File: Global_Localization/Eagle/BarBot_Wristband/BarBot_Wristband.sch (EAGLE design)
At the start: 2 parts, among them J1 AVR_SPI_PROG_3X2PTH, U2 DWM1000

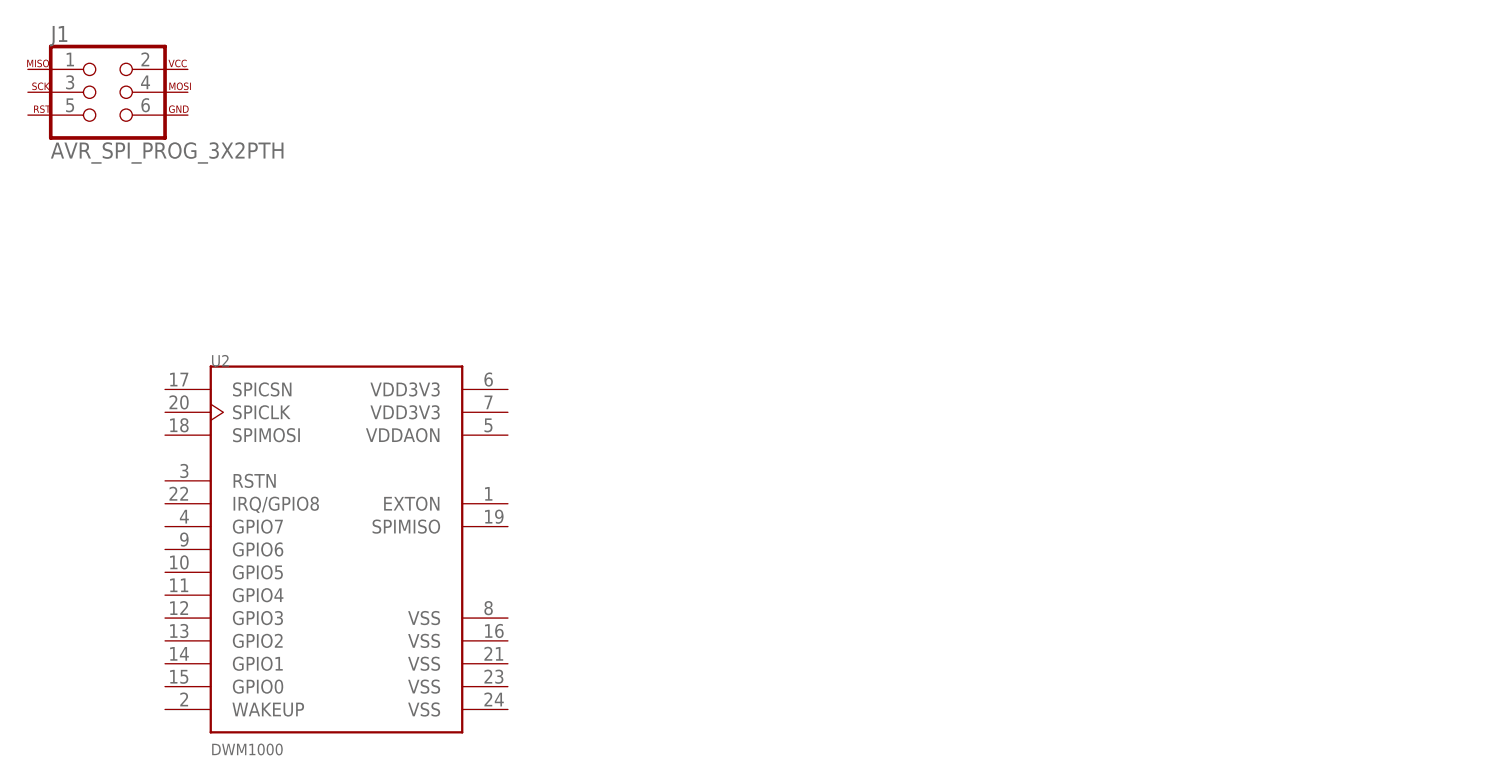
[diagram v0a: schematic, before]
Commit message: Updated board for wristband to be arduino shield
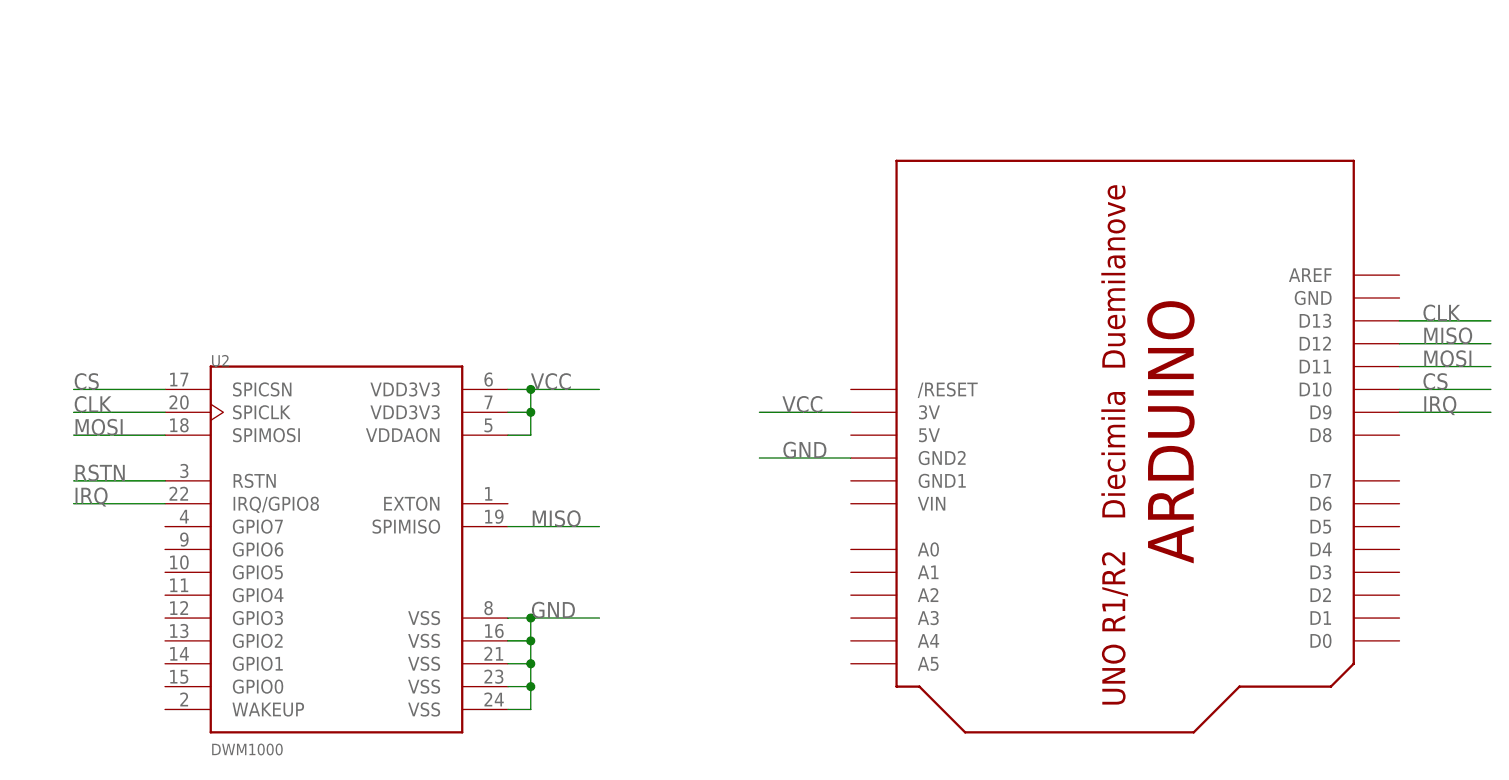
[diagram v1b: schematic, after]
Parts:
- removed J1: AVR_SPI_PROG_3X2PTH, SparkFun-Connectors:AVR_SPI_PROG_3X2PTH
- added U$1: ARDUINO-BPLACE, adafruit:ARDUINO-BPLACE
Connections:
- new net CLK: U$1.D13, U2.SPICLK
- new net CS: U$1.D10, U2.SPICSN
- new net GND: U$1.GND2, U2.VSS@1, U2.VSS@2, U2.VSS@3, U2.VSS@4, U2.VSS@5
- new net IRQ: U$1.D9, U2.IRQ/GPIO8
- new net MISO: U$1.D12, U2.SPIMISO
- new net MOSI: U$1.D11, U2.SPIMOSI
- new net RSTN: U2.RSTN
- new net VCC: U$1.3V, U2.VDD3V3@1, U2.VDD3V3@2, U2.VDDAON
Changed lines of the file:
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@@
 <layer number="230" name="230bmp" color="7" fill="1" visible="yes" active="yes"/>
 <layer number="231" name="231bmp" color="7" fill="1" visible="yes" active="yes"/>
+<layer number="232" name="Eagle3D_PG2" color="7" fill="1" visible="no" active="no"/>
+<layer number="233" name="Eagle3D_PG3" color="7" fill="1" visible="no" active="no"/>
 <layer number="248" name="Housing" color="7" fill="1" visible="yes" active="yes"/>
 <layer number="249" name="Edge" color="7" fill="1" visible="yes" active="yes"/>
@@
 <parts>
 <part name="U2" library="DWM1000" deviceset="DWM1000" device=""/>
-<part name="J1" library="SparkFun-Connectors" deviceset="AVR_SPI_PROG_3X2" device="PTH"/>
+<part name="U$1" library="adafruit" deviceset="ARDUINO" device="-BPLACE"/>
 </parts>
 <sheets>
@@
 <instances>
 <instance part="U2" gate="G$1" x="165.1" y="53.34"/>
-<instance part="J1" gate="G$1" x="139.7" y="104.14"/>
+<instance part="U$1" gate="G$1" x="256.54" y="73.66" rot="R270"/>
 </instances>
 <busses>
 </busses>
 <nets>
+<net name="MOSI" class="0">
+<segment>
+<pinref part="U2" gate="G$1" pin="SPIMOSI"/>
+<wire x1="147.32" y1="66.04" x2="137.16" y2="66.04" width="0.1524" layer="91"/>
+<label x="137.16" y="66.04" size="1.778" layer="95"/>
+</segment>
+<segment>
+<pinref part="U$1" gate="G$1" pin="D11"/>
+<wire x1="284.48" y1="73.66" x2="294.64" y2="73.66" width="0.1524" layer="91"/>
+<label x="287.02" y="73.66" size="1.778" layer="95"/>
+</segment>
+</net>
+<net name="CLK" class="0">
+<segment>
+<pinref part="U2" gate="G$1" pin="SPICLK"/>
+<wire x1="147.32" y1="68.58" x2="137.16" y2="68.58" width="0.1524" layer="91"/>
+<label x="137.16" y="68.58" size="1.778" layer="95"/>
+</segment>
+<segment>
+<pinref part="U$1" gate="G$1" pin="D13"/>
+<wire x1="284.48" y1="78.74" x2="294.64" y2="78.74" width="0.1524" layer="91"/>
+<label x="287.02" y="78.74" size="1.778" layer="95"/>
+</segment>
+</net>
+<net name="CS" class="0">
+<segment>
+<pinref part="U2" gate="G$1" pin="SPICSN"/>
+<wire x1="147.32" y1="71.12" x2="137.16" y2="71.12" width="0.1524" layer="91"/>
+<label x="137.16" y="71.12" size="1.778" layer="95"/>
+</segment>
+<segment>
+<pinref part="U$1" gate="G$1" pin="D10"/>
+<wire x1="284.48" y1="71.12" x2="294.64" y2="71.12" width="0.1524" layer="91"/>
+<label x="287.02" y="71.12" size="1.778" layer="95"/>
+</segment>
+</net>
+<net name="IRQ" class="0">
+<segment>
+<pinref part="U2" gate="G$1" pin="IRQ/GPIO8"/>
+<wire x1="147.32" y1="58.42" x2="137.16" y2="58.42" width="0.1524" layer="91"/>
+<label x="137.16" y="58.42" size="1.778" layer="95"/>
+</segment>
+<segment>
+<pinref part="U$1" gate="G$1" pin="D9"/>
+<wire x1="284.48" y1="68.58" x2="294.64" y2="68.58" width="0.1524" layer="91"/>
+<label x="287.02" y="68.58" size="1.778" layer="95"/>
+</segment>
+</net>
+<net name="MISO" class="0">
+<segment>
+<pinref part="U2" gate="G$1" pin="SPIMISO"/>
+<wire x1="185.42" y1="55.88" x2="195.58" y2="55.88" width="0.1524" layer="91"/>
+<label x="187.96" y="55.88" size="1.778" layer="95"/>
+</segment>
+<segment>
+<pinref part="U$1" gate="G$1" pin="D12"/>
+<wire x1="284.48" y1="76.2" x2="294.64" y2="76.2" width="0.1524" layer="91"/>
+<label x="287.02" y="76.2" size="1.778" layer="95"/>
+</segment>
+</net>
+<net name="GND" class="0">
+<segment>
+<pinref part="U2" gate="G$1" pin="VSS@5"/>
+<wire x1="185.42" y1="35.56" x2="187.96" y2="35.56" width="0.1524" layer="91"/>
+<wire x1="187.96" y1="35.56" x2="187.96" y2="38.1" width="0.1524" layer="91"/>
+<wire x1="187.96" y1="38.1" x2="187.96" y2="40.64" width="0.1524" layer="91"/>
+<wire x1="187.96" y1="40.64" x2="187.96" y2="43.18" width="0.1524" layer="91"/>
+<wire x1="187.96" y1="43.18" x2="187.96" y2="45.72" width="0.1524" layer="91"/>
+<wire x1="187.96" y1="45.72" x2="195.58" y2="45.72" width="0.1524" layer="91"/>
+<pinref part="U2" gate="G$1" pin="VSS@1"/>
+<wire x1="185.42" y1="45.72" x2="187.96" y2="45.72" width="0.1524" layer="91"/>
+<junction x="187.96" y="45.72"/>
+<pinref part="U2" gate="G$1" pin="VSS@2"/>
+<wire x1="185.42" y1="43.18" x2="187.96" y2="43.18" width="0.1524" layer="91"/>
+<junction x="187.96" y="43.18"/>
+<pinref part="U2" gate="G$1" pin="VSS@3"/>
+<wire x1="185.42" y1="40.64" x2="187.96" y2="40.64" width="0.1524" layer="91"/>
+<junction x="187.96" y="40.64"/>
+<pinref part="U2" gate="G$1" pin="VSS@4"/>
+<wire x1="185.42" y1="38.1" x2="187.96" y2="38.1" width="0.1524" layer="91"/>
+<junction x="187.96" y="38.1"/>
+<label x="187.96" y="45.72" size="1.778" layer="95"/>
+</segment>
+<segment>
+<pinref part="U$1" gate="G$1" pin="GND2"/>
+<wire x1="223.52" y1="63.5" x2="213.36" y2="63.5" width="0.1524" layer="91"/>
+<label x="215.9" y="63.5" size="1.778" layer="95"/>
+</segment>
+</net>
+<net name="VCC" class="0">
+<segment>
+<pinref part="U2" gate="G$1" pin="VDDAON"/>
+<wire x1="185.42" y1="66.04" x2="187.96" y2="66.04" width="0.1524" layer="91"/>
+<wire x1="187.96" y1="66.04" x2="187.96" y2="68.58" width="0.1524" layer="91"/>
+<wire x1="187.96" y1="68.58" x2="187.96" y2="71.12" width="0.1524" layer="91"/>
+<wire x1="187.96" y1="71.12" x2="195.58" y2="71.12" width="0.1524" layer="91"/>
+<pinref part="U2" gate="G$1" pin="VDD3V3@1"/>
+<wire x1="185.42" y1="71.12" x2="187.96" y2="71.12" width="0.1524" layer="91"/>
+<junction x="187.96" y="71.12"/>
+<pinref part="U2" gate="G$1" pin="VDD3V3@2"/>
+<wire x1="185.42" y1="68.58" x2="187.96" y2="68.58" width="0.1524" layer="91"/>
+<junction x="187.96" y="68.58"/>
+<label x="187.96" y="71.12" size="1.778" layer="95"/>
+</segment>
+<segment>
+<pinref part="U$1" gate="G$1" pin="3V"/>
+<wire x1="223.52" y1="68.58" x2="213.36" y2="68.58" width="0.1524" layer="91"/>
+<label x="215.9" y="68.58" size="1.778" layer="95"/>
+</segment>
+</net>
+<net name="RSTN" class="0">
+<segment>
+<pinref part="U2" gate="G$1" pin="RSTN"/>
+<wire x1="147.32" y1="60.96" x2="137.16" y2="60.96" width="0.1524" layer="91"/>
+<label x="137.16" y="60.96" size="1.778" layer="95"/>
+</segment>
+</net>
 </nets>
 </sheet>
